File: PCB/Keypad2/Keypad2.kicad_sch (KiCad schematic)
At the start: 21 parts, among them J1 Keypad, J2 Shelly, U1 SP3485, U2 ESP32-PICO-MINI-02, U3 LMR16006+FB, U4 QR

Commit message: PCb tweak
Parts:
- removed U3: LMR16006+FB, RevK:SOT-23-Thin-6-Reg, symbol RevK:LMR16006+FB
- added U2: LMR16006YDDCR, RevK:SOT-23-Thin-6-Reg, symbol RevK:LMR16006XDDCR
- C2: value 0.1uF -> 100nF; LCSC Part # (none) -> C30926; Note (none) -> X7R or X5R 0603
- C3: LCSC Part # (none) -> C19110; Note 0805 -> (none)
- C4: LCSC Part # (none) -> C17024; Note 1206 -> (none)
- D2: JLCPCB Rotation Offset (none) -> 180; LCSC Part # (none) -> C143805; Part No CD1206-B2100 -> (none)
- L1: LCSC Part # (none) -> C354575; Manufacturer Laird -> (none); Part No TYA4020 -> (none)
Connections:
- net +12V: now also U2.4 (SHDN), U2.5 (VIN)
- net +3V3: now also U2.7 (VOUT)
- net GND: now also U2.2 (GND)
- net at R5.2, R6.2: now also U2.3 (FB)
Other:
- moved on the sheet: R5, R6

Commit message: Tidy for production
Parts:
- removed D1: LED_RGBA, RevK:LED-RGB-1.6x1.6, symbol Device:LED_ARGB
- added D1: LED_BARG, RevK:MHS190RGBCT, symbol Device:LED_BARG
- R5: value 100k 1% or 0R -> 100k 1%; LCSC Part # (none) -> C14675
- R6: value 30k 1% or NF -> 30k 1%; LCSC Part # (none) -> C100001
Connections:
- net +3V3: now also D1.2 (A)
- net at R2.1: now also D1.3 (RK)
- net at R3.1: now also D1.4 (GK)
- net at R4.1: now also D1.1 (BK)
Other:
- moved on the sheet: C5

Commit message: Order boards
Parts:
- D1, D2: JLCPCB Rotation Offset 180 -> (none)
- U1: JLCPCB Rotation Offset (none) -> -90
- U2: JLCPCB Rotation Offset 0 -> 180
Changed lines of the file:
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@@
+      (effects (font (size 1.27 1.27)) hide)
+    )
+    (property "JLCPCB Rotation Offset" "-90" (at 114.3 152.4 0)
       (effects (font (size 1.27 1.27)) hide)
     )
@@
     )
     (property "LCSC Part #" "C409798" (at 190.5 88.9 0)
-      (effects (font (size 1.27 1.27)) hide)
-    )
-    (property "JLCPCB Rotation Offset" "180" (at 190.5 88.9 0)
       (effects (font (size 1.27 1.27)) hide)
     )
@@
       (effects (font (size 1.27 1.27)) hide)
     )
-    (property "JLCPCB Rotation Offset" "0" (at 221.615 132.715 0)
+    (property "JLCPCB Rotation Offset" "180" (at 221.615 132.715 0)
       (effects (font (size 1.27 1.27)) hide)
     )
@@
       (effects (font (size 1.27 1.27)) hide)
     )
-    (property "JLCPCB Rotation Offset" "180" (at 207.645 126.365 0)
-      (effects (font (size 1.27 1.27)) hide)
-    )

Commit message: Cap change
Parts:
- C1: value 10nF -> 1uF
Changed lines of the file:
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@@
       (effects (font (size 1.27 1.27)))
     )
-    (property "Value" "10nF" (at 95.7381 39.37 90)
+    (property "Value" "1uF" (at 95.7381 39.37 90)
       (effects (font (size 1.27 1.27)))
     )

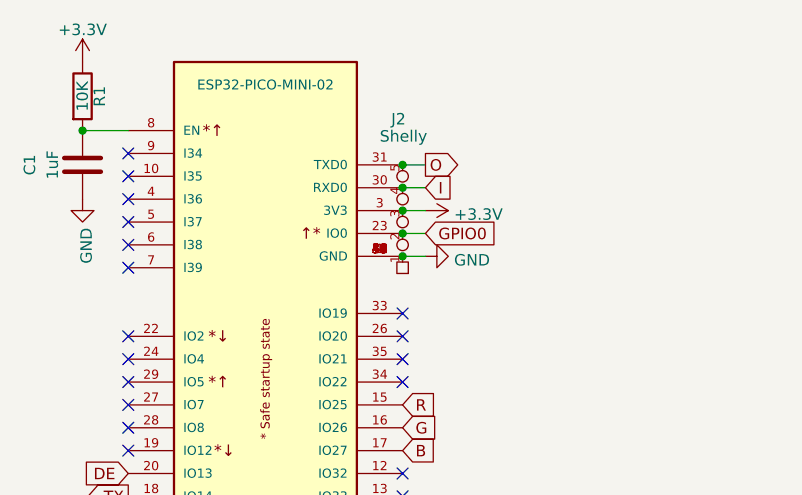
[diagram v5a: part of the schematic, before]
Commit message: Slight tidy, needs new LED/PSU/panel
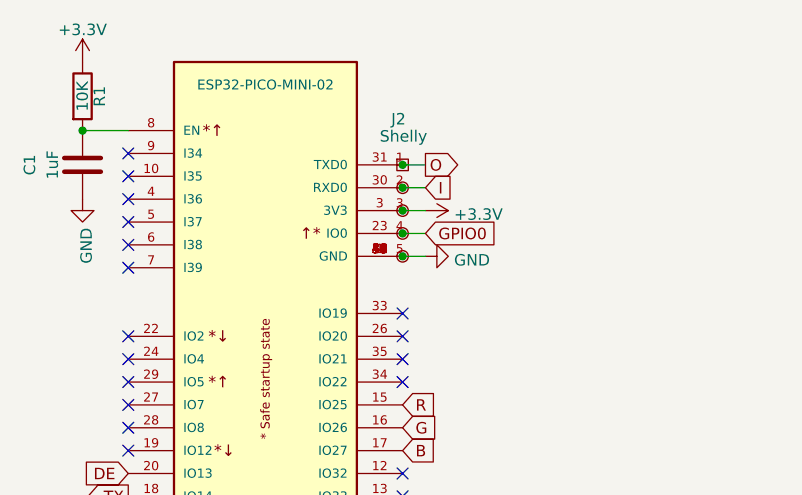
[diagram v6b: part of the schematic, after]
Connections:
- net GND: now also J2.5 (Tx); no longer J2.1 (GND)
- net GPIO0: now also J2.4 (Rx); no longer J2.2 (0)
- net I: now also J2.2 (0); no longer J2.4 (Rx)
- net O: now also J2.1 (GND); no longer J2.5 (Tx)
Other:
- moved on the sheet: J2
